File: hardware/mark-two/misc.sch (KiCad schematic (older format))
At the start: 12 parts, among them U2 MX6UL-VM

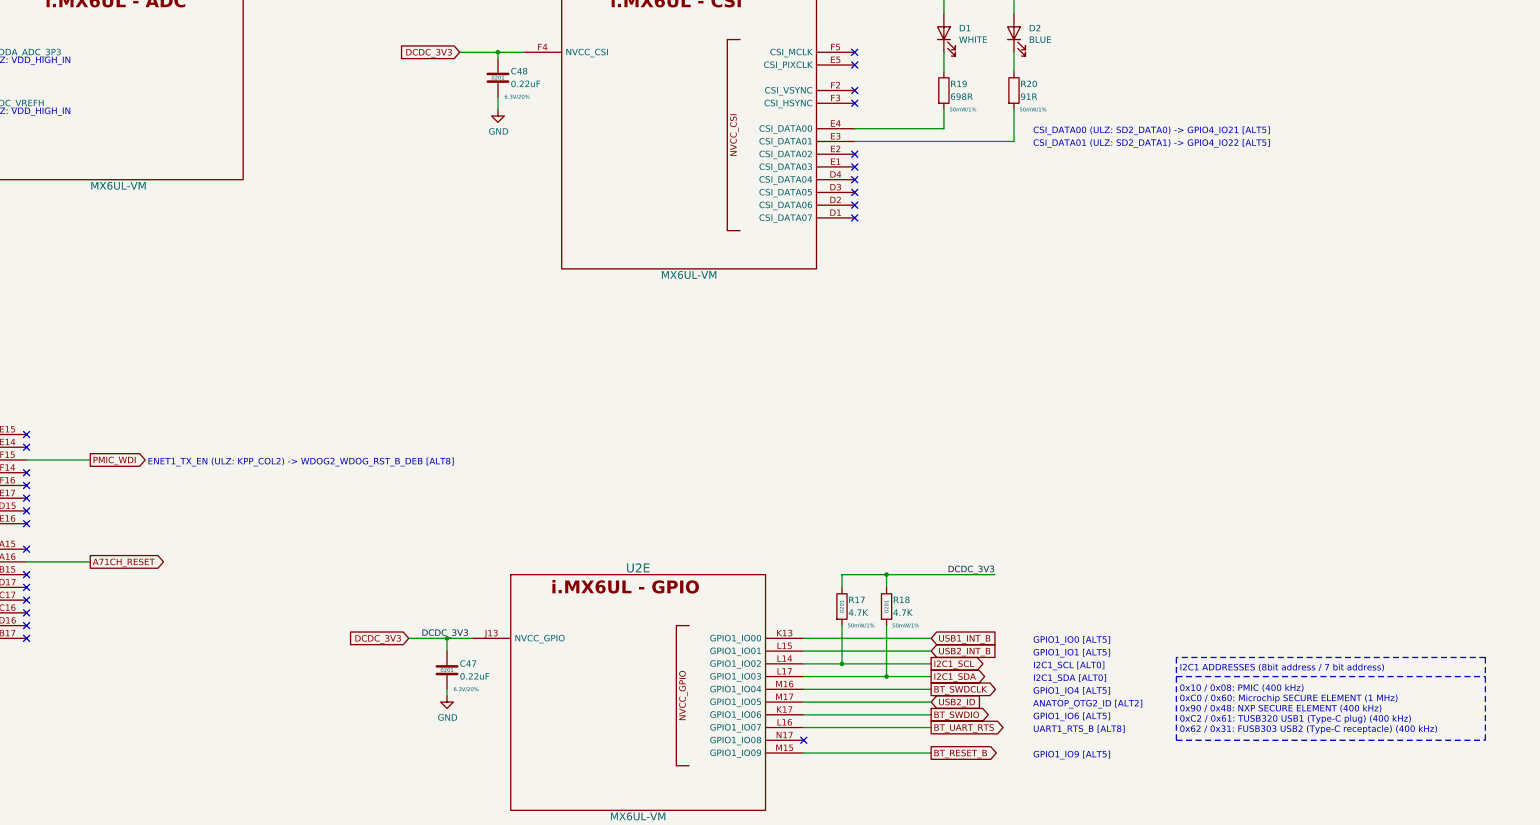
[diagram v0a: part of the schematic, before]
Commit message: add USB armory Mk II rev. γ
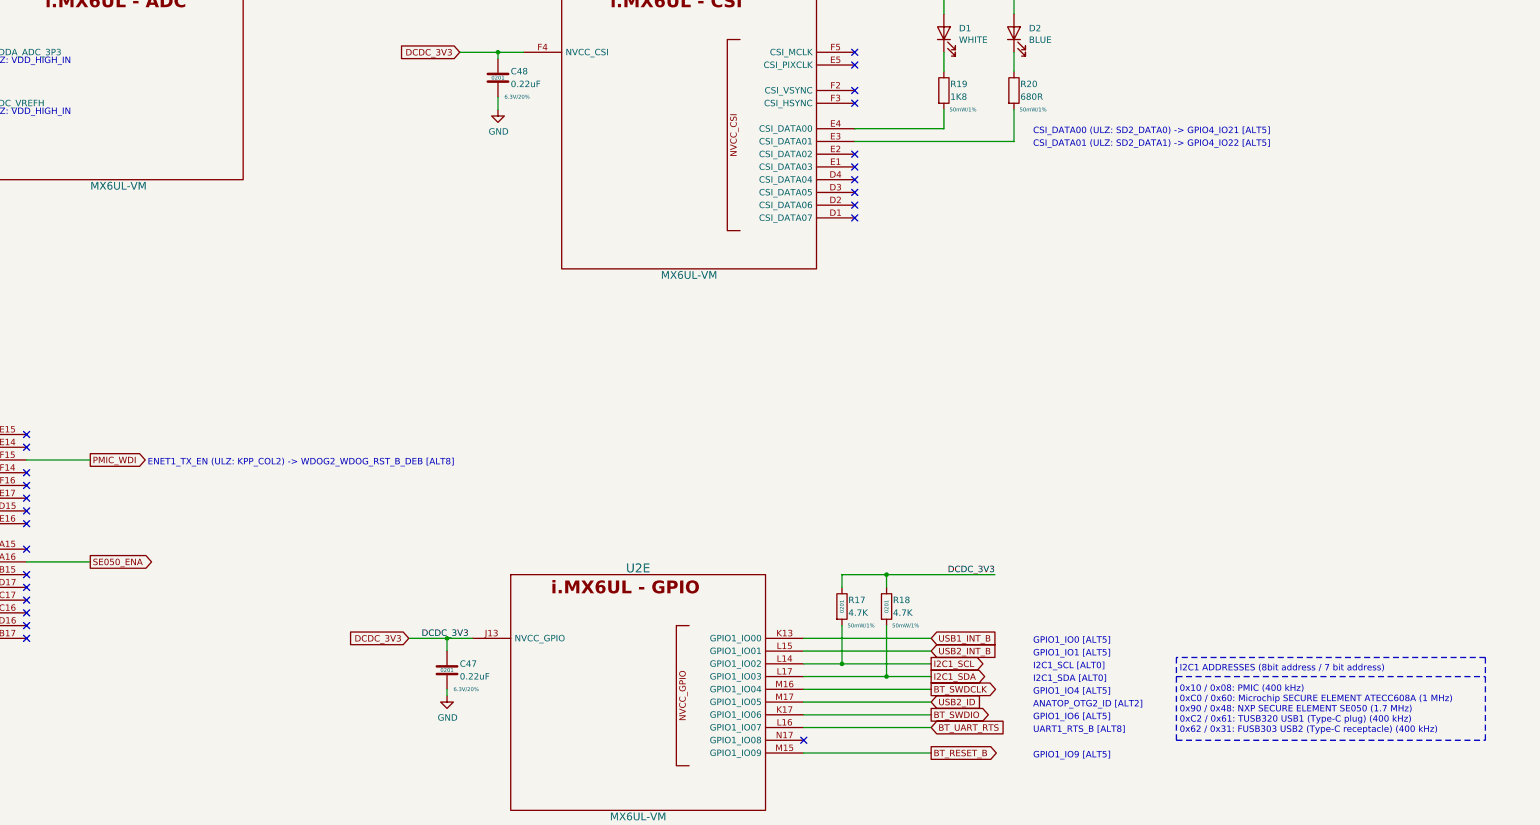
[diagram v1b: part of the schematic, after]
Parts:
- C38: Alternative PN (none) -> CL03A105KP3NSNC
- R19: value 698R -> 1K8; Mfg PN ERJ-1GEF6980C -> ERJ-1GNF1801C; Supplier PN P698ABTR-ND -> P122788CT-ND
- R20: value 91R -> 680R; Mfg PN ERJ-1GNF91R0C -> ERJ-1GNF6800C; Supplier PN P123203TR-ND -> P123124CT-ND
- U2: Mfg PN (none) -> MCIMX6Z0DVM09AB
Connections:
- net A71CH_RESET renamed SE050_ENA
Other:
- note added: "I2C1 ADDRESSES (8bit address / 7 bit address)\n\n0x10 / 0x08: PMIC (400 kHz)\n0xC0 / 0x60: Microchip SECURE ELEMENT ATECC608A (1 MHz)\n0x90 / 0x48: NXP SECURE ELEMENT SE050 (1.7 MHz)\n0xC2 / 0x61: TUSB320 USB1 (Type-C plug) (400 kHz)\n0x62 / 0x31: FUSB303 USB2 (Type-C receptacle) (400 kHz)"
- note removed: "I2C1 ADDRESSES (8bit address / 7 bit address)\n\n0x10 / 0x08: PMIC (400 kHz)\n0xC0 / 0x60: Microchip SECURE ELEMENT (1 MHz)\n0x90 / 0x48: NXP SECURE ELEMENT (400 kHz)\n0xC2 / 0x61: TUSB320 USB1 (Type-C plug) (400 kHz)\n0x62 / 0x31: FUSB303 USB2 (Type-C receptacle) (400 kHz)"
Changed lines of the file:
@@
 EESchema Schematic File Version 4
-LIBS:armory-cache
 EELAYER 30 0
 EELAYER END
@@
 encoding utf-8
 Sheet 4 13
-Title "USB ARMORY"
-Date "2019-06-25"
-Rev "MARK II"
+Title "USB armory Mk II"
+Date "2021-02-18"
+Rev "γ"
 Comp "F-Secure"
-Comment1 "Copyright © 2019 F-Secure"
-Comment2 "License: CERN OHL v1.2"
-Comment3 "https://github.com/inversepath/usbarmory"
+Comment1 "Copyright © F-Secure Corporation"
+Comment2 "License: CERN-OHL-S"
+Comment3 "https://github.com/f-secure-foundry/usbarmory"
 Comment4 ""
 $EndDescr
@@
 F 2 "armory-kicad:SOT1534-2" H 5510 340 60  0001 C CNN
 F 3 "https://www.nxp.com/docs/en/data-sheet/IMX6ULCEC.pdf" H 5510 340 60  0001 C CNN
+F 4 "MCIMX6Z0DVM09AB" H 5000 1500 50  0001 C CNN "Mfg PN"
 	10   5000 1500
 	1    0    0    -1
@@
 F 2 "armory-kicad:SOT1534-2" H 3510 3340 60  0001 C CNN
 F 3 "https://www.nxp.com/docs/en/data-sheet/IMX6ULCEC.pdf" H 3510 3340 60  0001 C CNN
+F 4 "MCIMX6Z0DVM09AB" H 3000 4500 50  0001 C CNN "Mfg PN"
 	6    3000 4500
 	1    0    0    -1
@@
 F 2 "armory-kicad:SOT1534-2" H 9610 4940 60  0001 C CNN
 F 3 "https://www.nxp.com/docs/en/data-sheet/IMX6ULCEC.pdf" H 9610 4940 60  0001 C CNN
+F 4 "MCIMX6Z0DVM09AB" H 9100 6100 50  0001 C CNN "Mfg PN"
 	5    9100 6100
 	1    0    0    -1
@@
 F 2 "armory-kicad:SOT1534-2" H 10010 340 60  0001 C CNN
 F 3 "https://www.nxp.com/docs/en/data-sheet/IMX6ULCEC.pdf" H 10010 340 60  0001 C CNN
+F 4 "MCIMX6Z0DVM09AB" H 9500 1500 50  0001 C CNN "Mfg PN"
 	4    9500 1500
 	1    0    0    -1
@@
 	10700 6800 11400 6800
 Text Notes 13350 7350 0    50   ~ 0
-I2C1 ADDRESSES (8bit address / 7 bit address)\n\n0x10 / 0x08: PMIC (400 kHz)\n0xC0 / 0x60: Microchip SECURE ELEMENT (1 MHz)\n0x90 / 0x48: NXP SECURE ELEMENT (400 kHz)\n0xC2 / 0x61: TUSB320 USB1 (Type-C plug) (400 kHz)\n0x62 / 0x31: FUSB303 USB2 (Type-C receptacle) (400 kHz)
+I2C1 ADDRESSES (8bit address / 7 bit address)\n\n0x10 / 0x08: PMIC (400 kHz)\n0xC0 / 0x60: Microchip SECURE ELEMENT ATECC608A (1 MHz)\n0x90 / 0x48: NXP SECURE ELEMENT SE050 (1.7 MHz)\n0xC2 / 0x61: TUSB320 USB1 (Type-C plug) (400 kHz)\n0x62 / 0x31: FUSB303 USB2 (Type-C receptacle) (400 kHz)
 Text GLabel 11400 6600 2    50   Input ~ 0
 USB1_INT_B
@@
 F 9 "0201" H 2700 2250 30  0000 C CNN "FP"
 F 10 "10V/20%" H 2850 2100 30  0000 C CNN "Rating"
+F 11 "CL03A105KP3NSNC" H 2700 2250 50  0001 C CNN "Alternative PN"
 	1    2700 2250
 	1    0    0    -1
@@
 AR Path="/53834030/5C8E0E0A" Ref="R19"  Part="1"
 F 0 "R19" H 11550 2350 50  0000 L CNN
-F 1 "698R" H 11550 2250 50  0000 L CNN
+F 1 "1K8" H 11550 2250 50  0000 L CNN
 F 2 "armory-kicad:SM0201" V 11430 2300 50  0001 C CNN
 F 3 "~" H 11500 2300 50  0001 C CNN
 F 4 "Panasonic Electronic Components" H 11500 2300 50  0001 C CNN "Mfg"
-F 5 "ERJ-1GEF6980C" H 11500 2300 50  0001 C CNN "Mfg PN"
+F 5 "ERJ-1GNF1801C" H 11500 2300 50  0001 C CNN "Mfg PN"
 F 6 "1%, 50mW" H 11500 2300 50  0001 C CNN "Desc"
 F 7 "Digikey" H 11500 2300 50  0001 C CNN "Supplier"
-F 8 "P698ABTR-ND" H 11500 2300 50  0001 C CNN "Supplier PN"
+F 8 "P122788CT-ND" H 11500 2300 50  0001 C CNN "Supplier PN"
 F 9 "50mW/1%" H 11650 2150 30  0000 C CNN "Rating"
 F 10 "0201" H 0   0   50  0001 C CNN "FP"
@@
 AR Path="/53834030/5C8E1BA1" Ref="R20"  Part="1"
 F 0 "R20" H 12100 2350 50  0000 L CNN
-F 1 "91R" H 12100 2250 50  0000 L CNN
+F 1 "680R" H 12100 2250 50  0000 L CNN
 F 2 "armory-kicad:SM0201" V 11980 2300 50  0001 C CNN
 F 3 "~" H 12050 2300 50  0001 C CNN
 F 4 "Panasonic Electronic Components" H 12050 2300 50  0001 C CNN "Mfg"
-F 5 "ERJ-1GNF91R0C" H 12050 2300 50  0001 C CNN "Mfg PN"
+F 5 "ERJ-1GNF6800C" H 12050 2300 50  0001 C CNN "Mfg PN"
 F 6 "1%, 50mW" H 12050 2300 50  0001 C CNN "Desc"
 F 7 "Digikey" H 12050 2300 50  0001 C CNN "Supplier"
-F 8 "P123203TR-ND" H 12050 2300 50  0001 C CNN "Supplier PN"
+F 8 "P123124CT-ND" H 12050 2300 50  0001 C CNN "Supplier PN"
 F 9 "50mW/1%" H 12200 2150 30  0000 C CNN "Rating"
 F 10 "0201" H 0   0   50  0001 C CNN "FP"
@@
 Wire Wire Line
 	7600 7000 7600 7050
-Text GLabel 11400 7300 2    50   Output ~ 0
+Text GLabel 11400 7300 2    50   Input ~ 0
 BT_UART_RTS
 Wire Wire Line
@@
 ULZ: VDD_HIGH_IN
 Text GLabel 4800 6000 2    50   Output ~ 0
-A71CH_RESET
+SE050_ENA
 Wire Wire Line
 	4800 6000 4300 6000
